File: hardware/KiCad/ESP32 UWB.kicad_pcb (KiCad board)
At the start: 2 copper layers, 72.3 x 32.6 mm, 56 parts, among them J1 HEADER-20P-2.54, J2 HEADER-12P-2.54, J3 10118194-0001LF, Q1 S8050, Q2 S8050, SW1 BUTTON, SW2 BUTTON, U1 AMS1117-3.3, U2 ESP32-C3-MINI-1-N4, U3 SILICON_LABS_CP2102N-A01-GQFN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

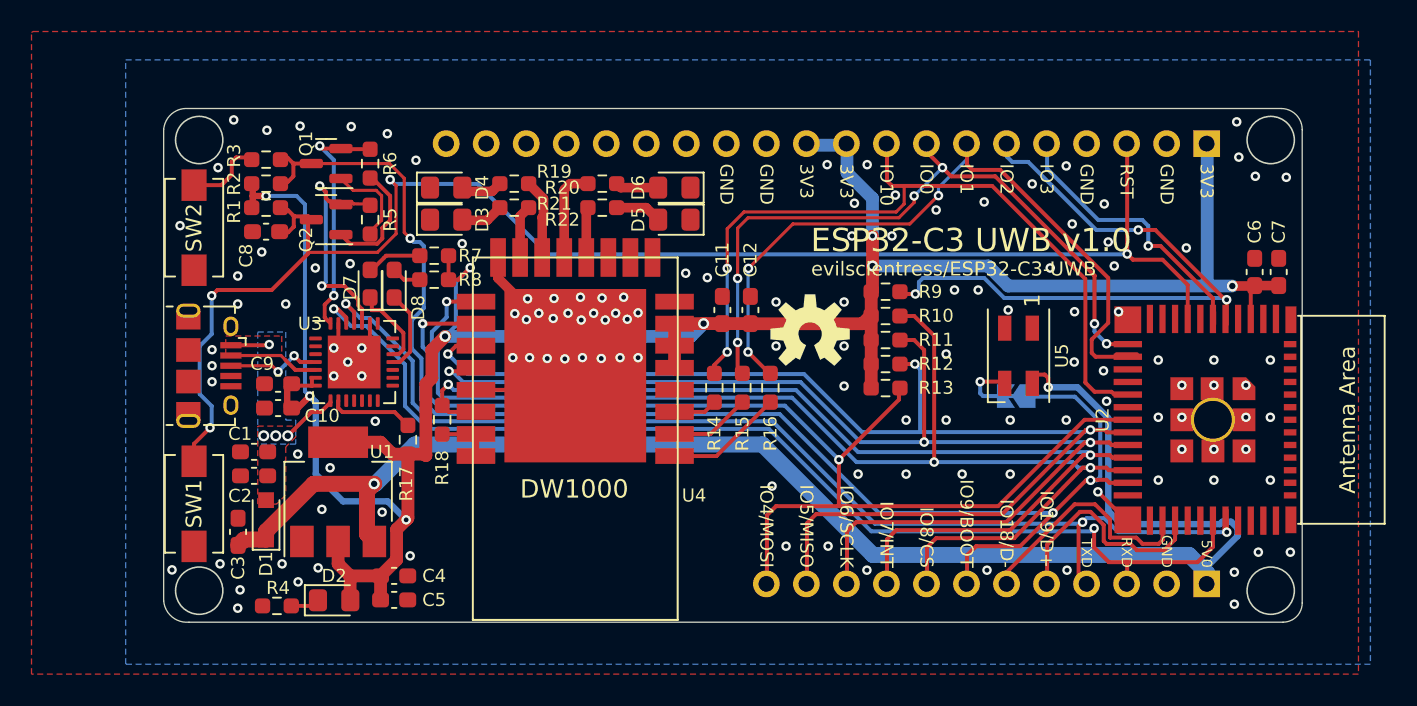
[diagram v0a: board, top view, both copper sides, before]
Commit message: add keepout zone and labels for LEDs
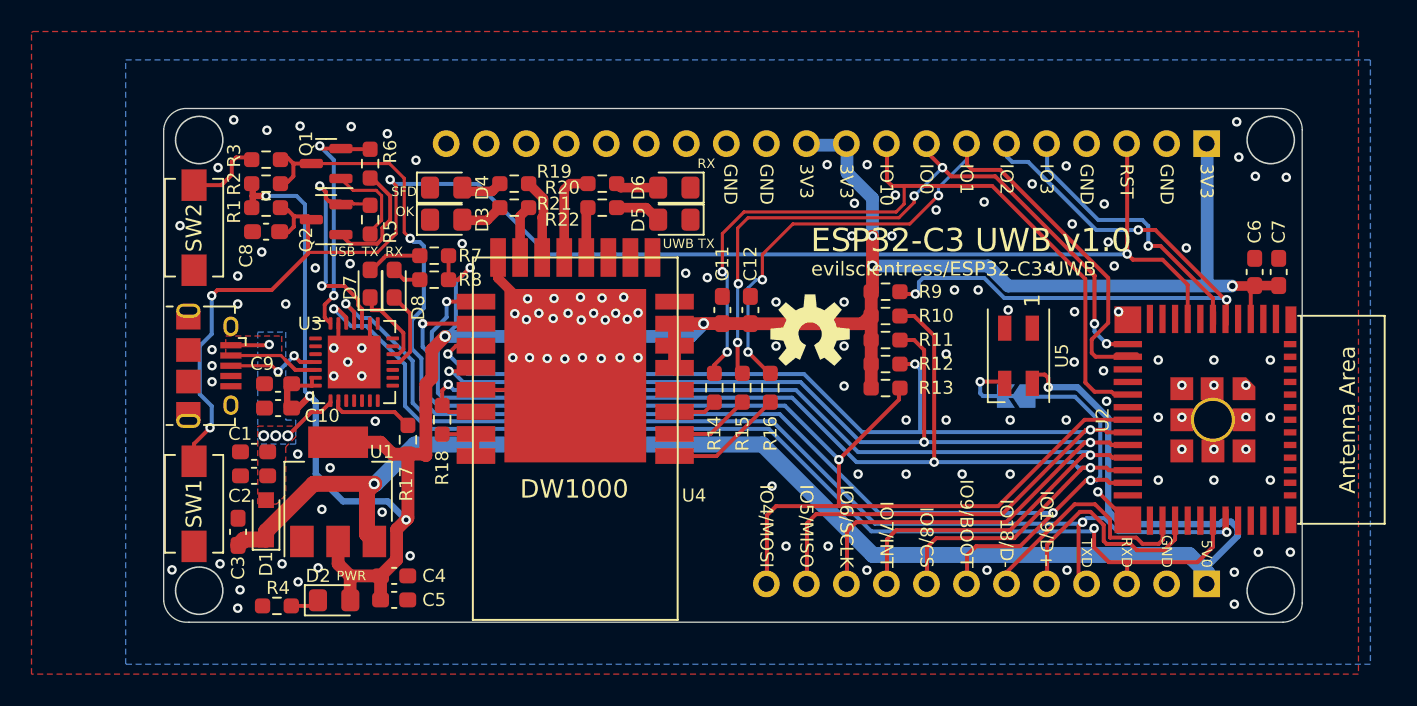
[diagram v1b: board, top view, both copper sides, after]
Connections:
- net /D+ renamed D+
- net /D- renamed D-
- net /DTR renamed DTR
- net /IO0 renamed IO0
- net /IO1 renamed IO1
- net /IO10 renamed IO10
- net /IO18 renamed IO18
- net /IO19 renamed IO19
- net /IO2 renamed IO2
- net /IO3 renamed IO3
- net /IO4/MOSI renamed IO4/MOSI
- net /IO5/MISO renamed IO5/MISO
- net /IO6/SCLK renamed IO6/SCLK
- net /IO7 renamed IO7
- net /IO8/CS renamed IO8/CS
- net /IO9 renamed IO9
- net /LEDRX renamed LEDRX
- net /LEDRXOK renamed LEDRXOK
- net /LEDSFD renamed LEDSFD
- net /LEDTX renamed LEDTX
- net /RTS renamed RTS
- net /RXD renamed RXD
- net /TXD renamed TXD
- net /VDD5V renamed +5V
- C8 pad 1: /RESET -> RESET
- J1 pad 3: /RESET -> RESET
- Q2 pad 3: /RESET -> RESET
- R1 pad 1: /RESET -> RESET
- SW1 pad 1: GND -> RESET
- SW1 pad 2: /RESET -> GND
- SW2 pad 1: GND -> Net-(R3-Pad1)
- SW2 pad 2: Net-(R3-Pad1) -> GND
- U2 pad 8: /RESET -> RESET
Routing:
- net RESET: track 0.00 -> 97.2 mm, vias 0 -> 4
- net /RESET: track 97.2 -> 0.00 mm, vias 4 -> 0
- net GND: vias 130 -> 131
- net DTR: vias 3 -> 2
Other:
- board text added: "OK"
- board text added: "PWR"
- board text added: "RX"
- board text added: "SFD"
- board text added: "TX"
- board text added: "USB"
- board text added: "UWB"

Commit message: make DRC happy
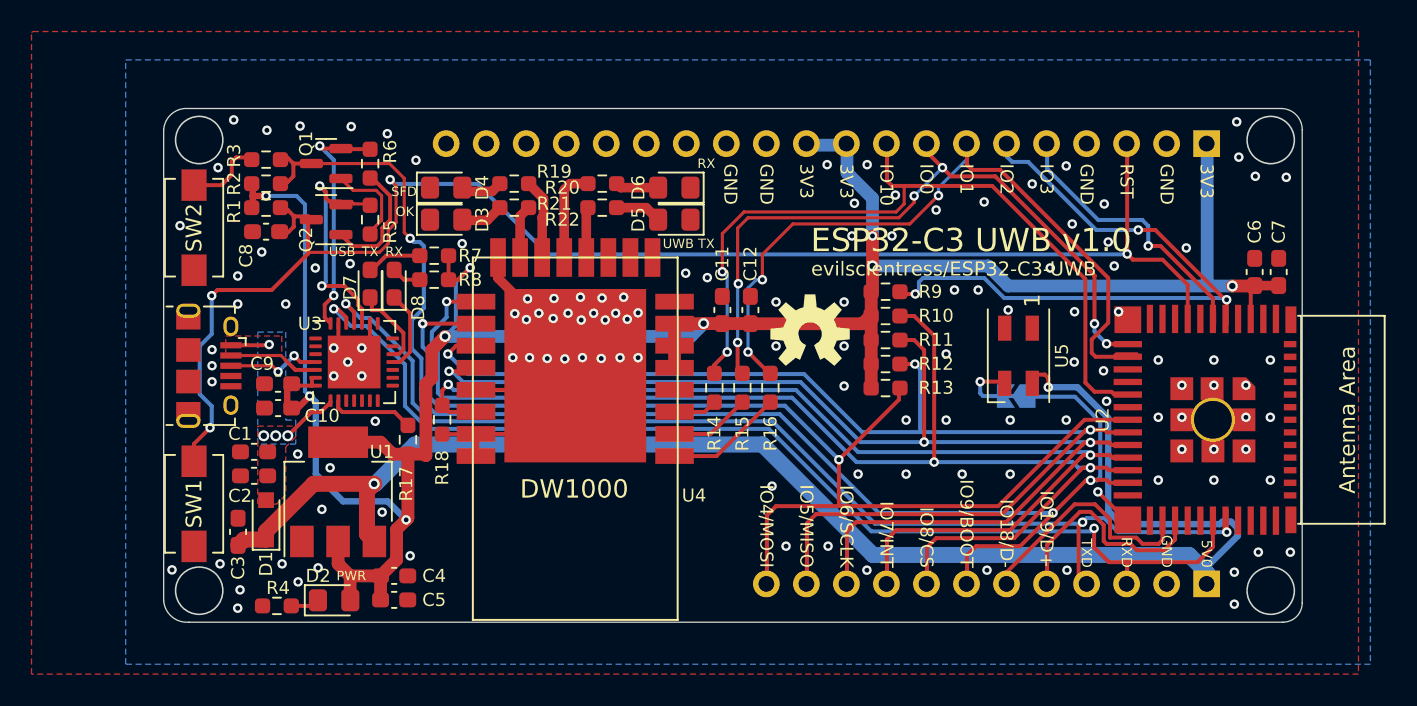
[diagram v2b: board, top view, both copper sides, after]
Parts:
- turned SW1 to -90 degrees
- turned SW2 to -90 degrees
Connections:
- U4 pad GND: (no net) -> GND
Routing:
- net GND: track 19.7 -> 26.3 mm

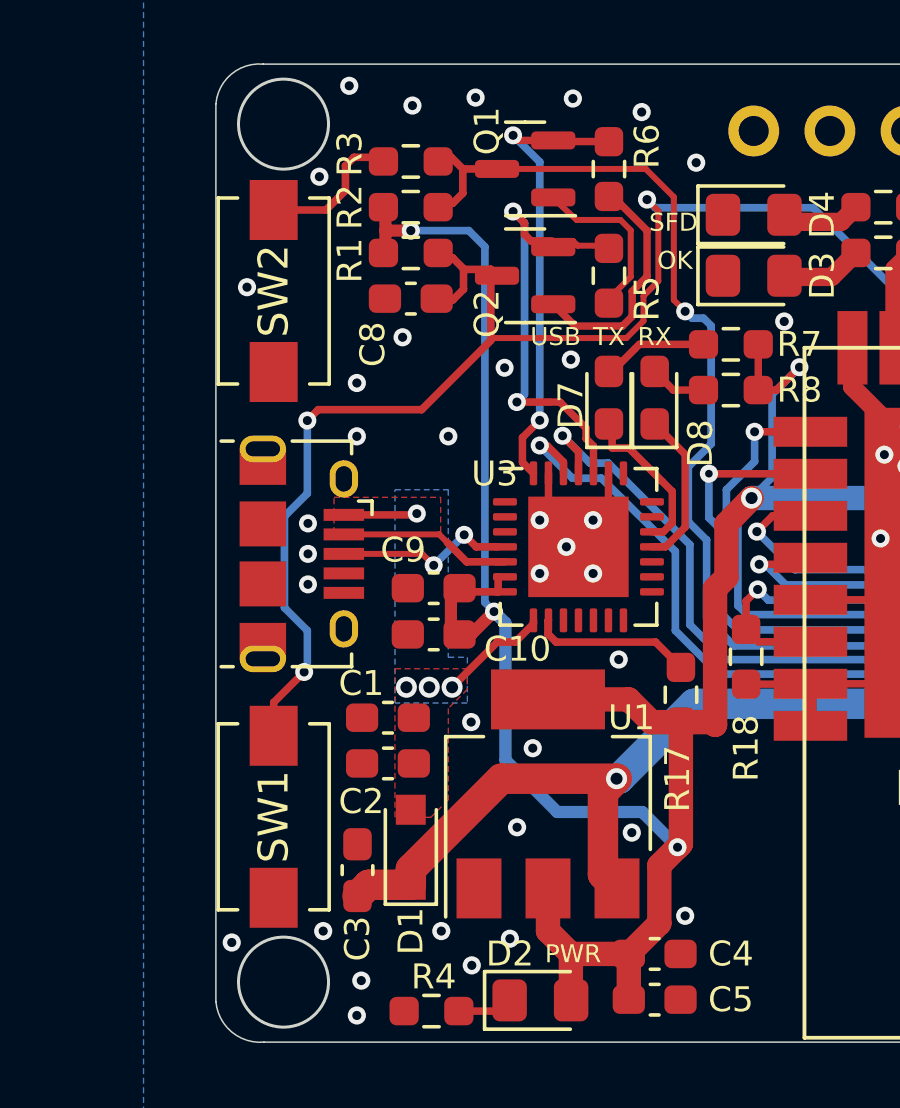
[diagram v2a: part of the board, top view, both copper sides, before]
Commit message: further cleanup and improvment of the KiCad version of the PCB
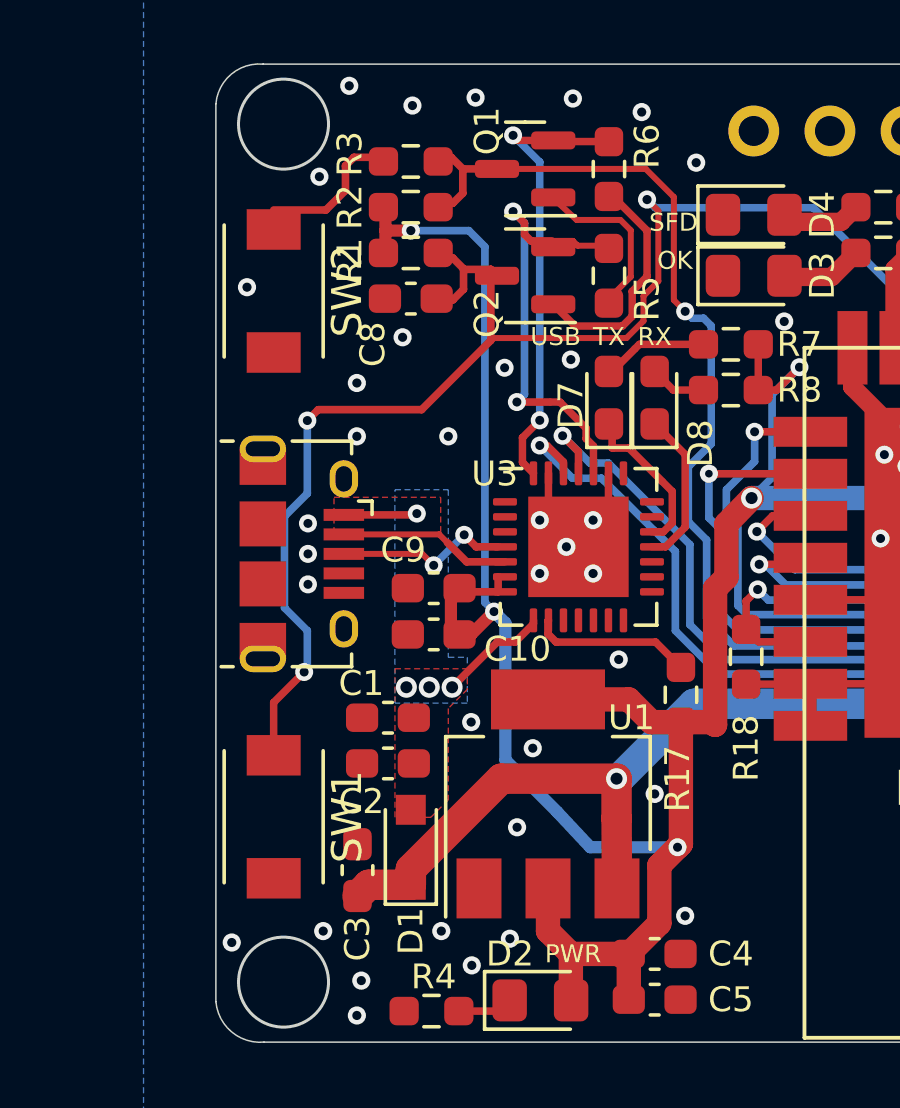
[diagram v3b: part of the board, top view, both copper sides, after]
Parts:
- SW1, SW2: footprint Button_Switch_SMD:SW_SPST_EVQPE1 -> ESP32 UWB:SW_Push_3x4mm
- U4: value DWM1000 -> Val**

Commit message: label buttons
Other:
- board text added: "FLASH"
- board text added: "RESET"
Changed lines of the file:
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@@
     (property "Sheetname" "")
     (attr smd)
-    (fp_text reference "SW2" (at 0 -2.45 -90) (layer "F.SilkS")
+    (fp_text reference "SW2" (at 0 0 -90) (layer "F.SilkS")
       (effects (font (size 1 1) (thickness 0.15)))
     )
@@
     (property "Sheetname" "")
     (attr smd)
-    (fp_text reference "SW1" (at 0 -2.45 -90) (layer "F.SilkS")
+    (fp_text reference "SW1" (at 0 0 -90) (layer "F.SilkS")
       (effects (font (size 1 1) (thickness 0.15)))
     )
@@
     (effects (font (size 0.666496 0.666496) (thickness 0.146304)) (justify right))
   )
+  (gr_text "FLASH" (at 114.3 99.568) (layer "F.SilkS")
+    (effects (font (size 0.6 0.6) (thickness 0.1)))
+  )
   (gr_text "ESP32-C3 UWB v1.0" (at 153.4344 97.933155) (layer "F.SilkS")
     (effects (font (size 1.475232 1.475232) (thickness 0.201168)) (justify left bottom))
@@
     (effects (font (size 0.83312 0.83312) (thickness 0.18288)) (justify left))
   )
+  (gr_text "RESET" (at 114.3 117.094) (layer "F.SilkS")
+    (effects (font (size 0.6 0.6) (thickness 0.1)))
+  )
   (gr_text "UWB" (at 145.034 97.282) (layer "F.SilkS")

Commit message: add JLCJLCJLCJLC
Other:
- board text added: "JLCJLCJLCJLC"
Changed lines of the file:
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@@
     (effects (font (size 0.66 0.66) (thickness 0.146)) (justify right))
+  )
+  (gr_text "JLCJLCJLCJLC" (at 138.43 116.84) (layer "F.SilkS")
+    (effects (font (size 0.85 0.85) (thickness 0.2)))
   )
   (gr_text "GND" (at 150.622 92.202 270) (layer "F.SilkS")
